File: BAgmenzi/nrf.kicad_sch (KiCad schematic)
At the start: 1 part, among them M1 *

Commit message: added libraries, other changes in sch, started pcb
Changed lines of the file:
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@@
+		)
+	)
+	(hierarchical_label "PPG_I2C{SCL, SDA}"
+		(shape bidirectional)
+		(at 63.5 114.3 180)
+		(effects
+			(font
+				(size 1.27 1.27)
+			)
+			(justify right)
 		)
 	)

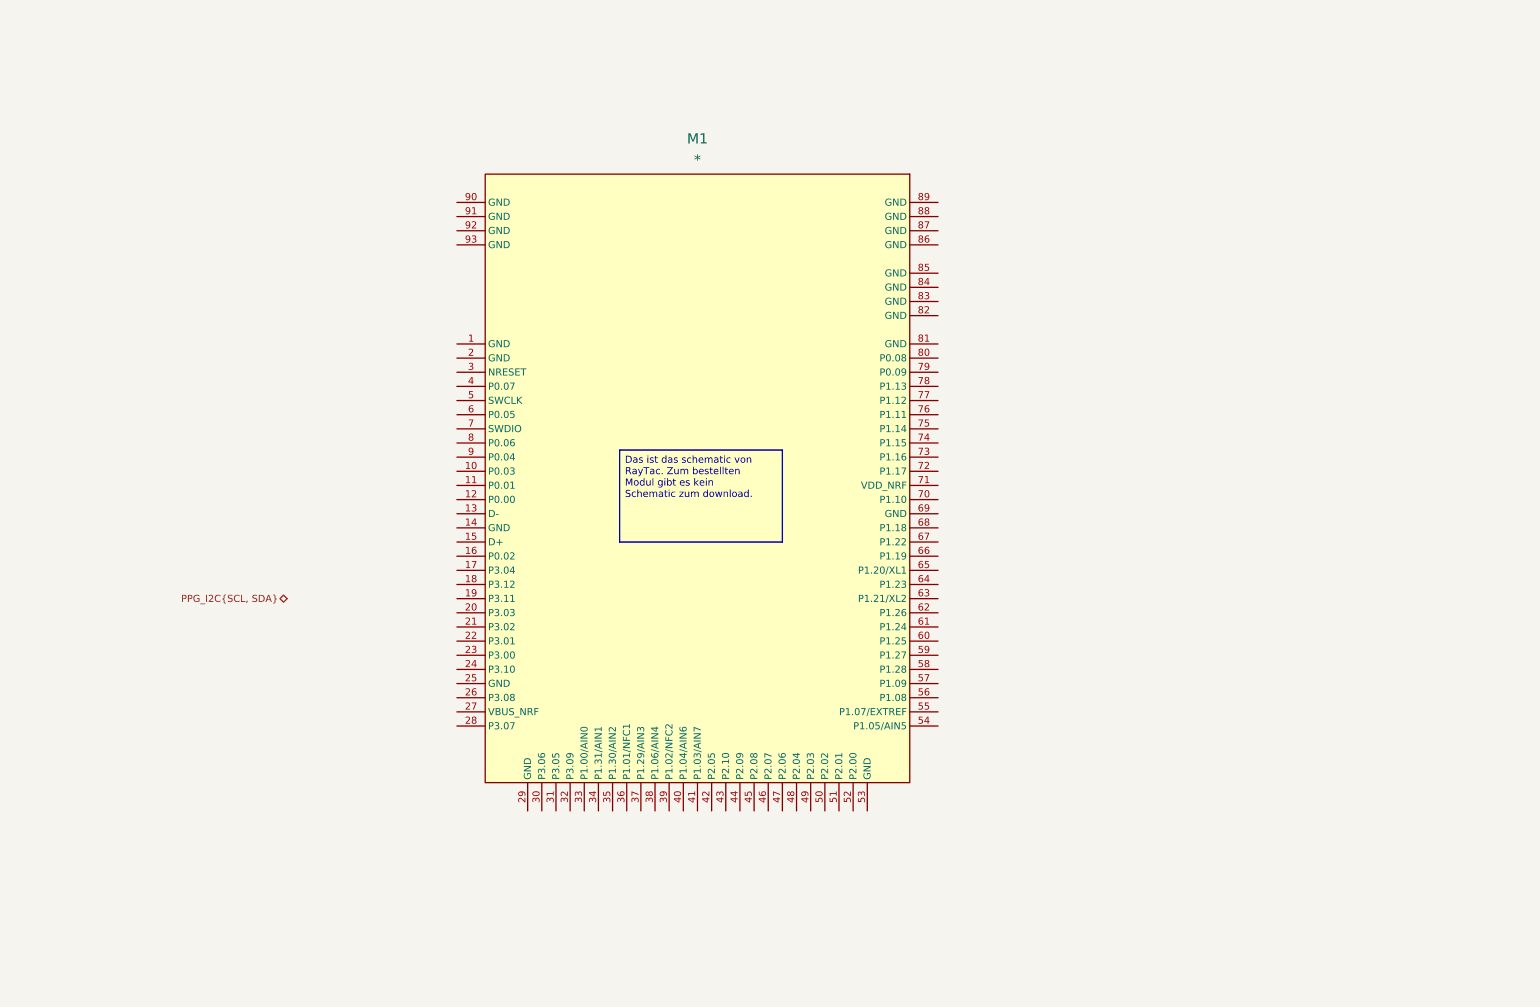
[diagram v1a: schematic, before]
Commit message: changed VRX rail and deleted U12
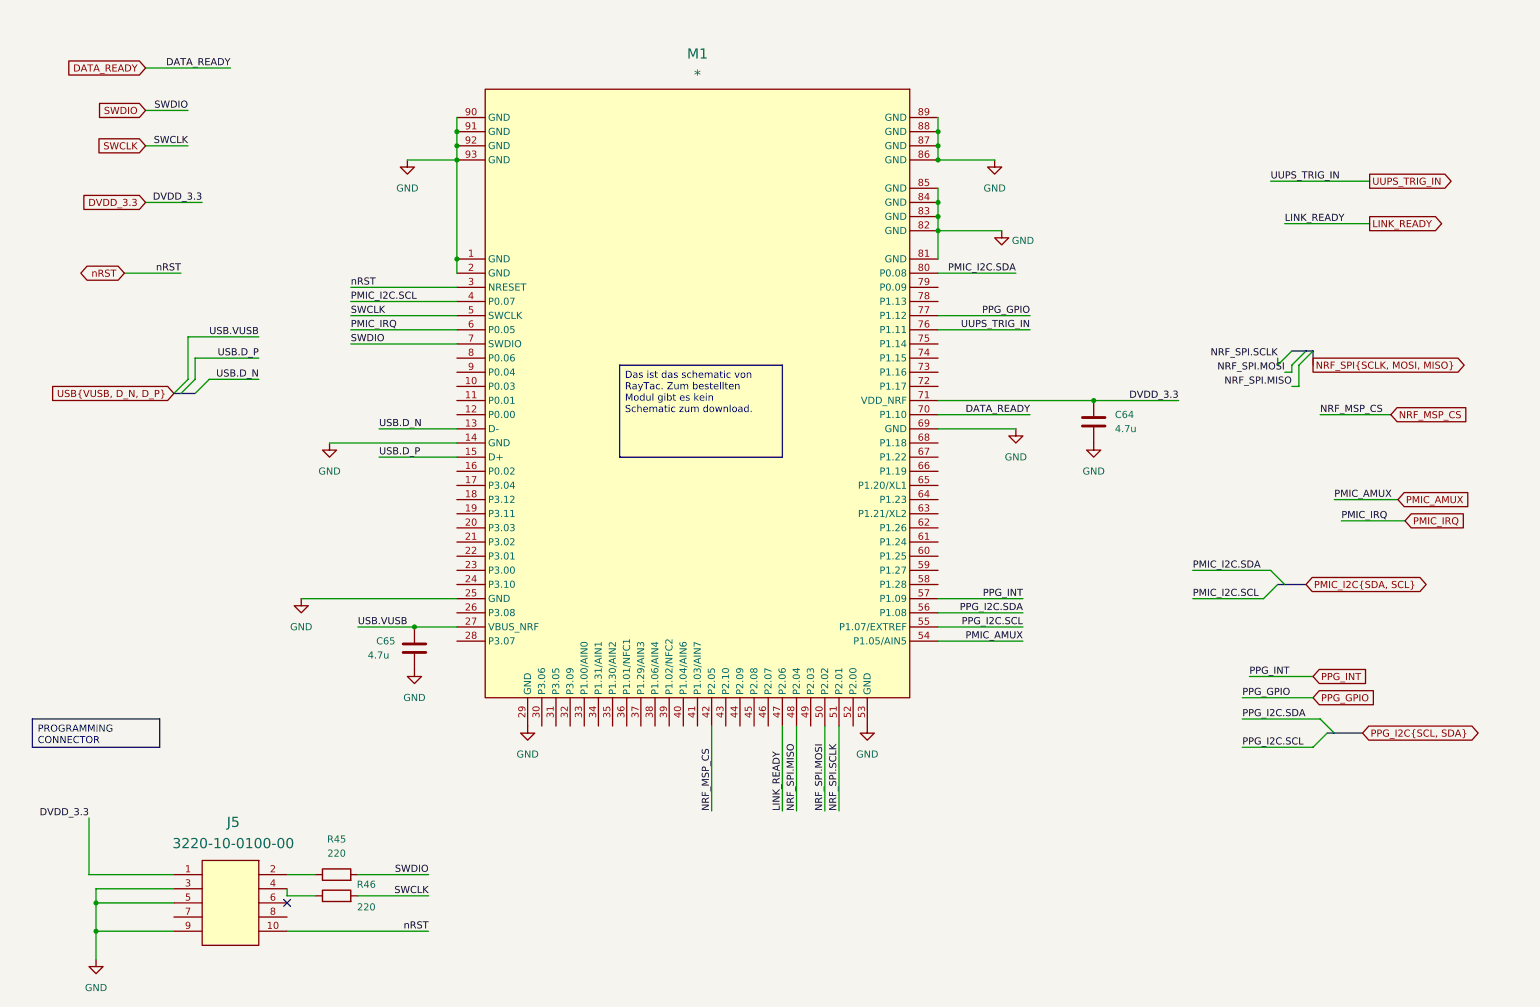
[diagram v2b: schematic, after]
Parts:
- added C64, C65: 4.7u, Capacitor_SMD:C_0402_1005Metric, symbol Device:C
- added J5: 3220-10-0100-00, EEG_PcbLib.PcbLib:CONN_3220-10-0100-00_CNC, symbol EEG_SchLib:3220-10-0100-00
- added R45, R46: 220, symbol Device:R
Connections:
- net GND: now reaches M1.1 (GND)
- net GND: now also M1.14 (GND), M1.2 (GND), M1.25 (GND), M1.29 (GND), M1.53 (GND), M1.69 (GND), M1.81 (GND), M1.82 (GND), M1.83 (GND), M1.84 (GND), M1.85 (GND), M1.86 (GND), M1.87 (GND), M1.88 (GND), M1.89 (GND), M1.90 (GND), M1.91 (GND), M1.92 (GND), M1.93 (GND), C64.2, C65.2, J5.3, J5.5, J5.9
- net USB.D_N: now reaches M1.13 (D-)
- net USB.D_P: now reaches M1.15 (D+)
- net USB.VUSB: now reaches M1.27 (VBUS_NRF)
- net USB.VUSB: now also C65.1
- net nRST: now reaches M1.3 (NRESET)
- net nRST: now also J5.10
- net PMIC_I2C.SCL: now reaches M1.4 (P0.07)
- net NRF_MSP_CS: now reaches M1.42 (P2.05)
- net LINK_READY: now reaches M1.47 (P2.06)
- net NRF_SPI.MISO: now reaches M1.48 (P2.04)
- net SWCLK: now reaches M1.5 (SWCLK)
- net SWCLK: now also R46.2
- net NRF_SPI.MOSI: now reaches M1.50 (P2.02)
- net NRF_SPI.SCLK: now reaches M1.51 (P2.01)
- net PMIC_AMUX: now reaches M1.54 (P1.05/AIN5)
- net PPG_I2C.SCL: now reaches M1.55 (P1.07/EXTREF)
- net PPG_I2C.SDA: now reaches M1.56 (P1.08)
- net PPG_INT: now reaches M1.57 (P1.09)
- net PMIC_IRQ: now reaches M1.6 (P0.05)
- net SWDIO: now reaches M1.7 (SWDIO)
- net SWDIO: now also R45.2
- net DATA_READY: now reaches M1.70 (P1.10)
- net DVDD_3.3: now reaches M1.71 (VDD_NRF)
- net DVDD_3.3: now also C64.1, J5.1
- net UUPS_TRIG_IN: now reaches M1.76 (P1.11)
- net PPG_GPIO: now reaches M1.77 (P1.12)
- net PMIC_I2C.SDA: now reaches M1.80 (P0.08)
- new net: J5.4, R46.1
- new net: J5.2, R45.1
- no-connect marks 0 -> 1
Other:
- moved on the sheet: M1

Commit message: started layout, front v backside
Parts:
- J5: footprint EEG_PcbLib.PcbLib:CONN_3220-10-0100-00_CNC -> EEG_PcbLib:CONN_3220-10-0100-00_CNC
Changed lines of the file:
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@@
 			)
 		)
-		(property "Footprint" "EEG_PcbLib.PcbLib:CONN_3220-10-0100-00_CNC"
+		(property "Footprint" "EEG_PcbLib:CONN_3220-10-0100-00_CNC"
 			(at 53.34 168.91 0)
 			(effects

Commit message: started routing, changed enable signals to nRF
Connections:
- net HV_NEG_EN: now reaches M1.72 (P1.17)
- net HV_POS_EN: now reaches M1.73 (P1.16)
- net HV_PWR_EN: now reaches M1.74 (P1.15)
- net VRX_EN: now reaches M1.75 (P1.14)

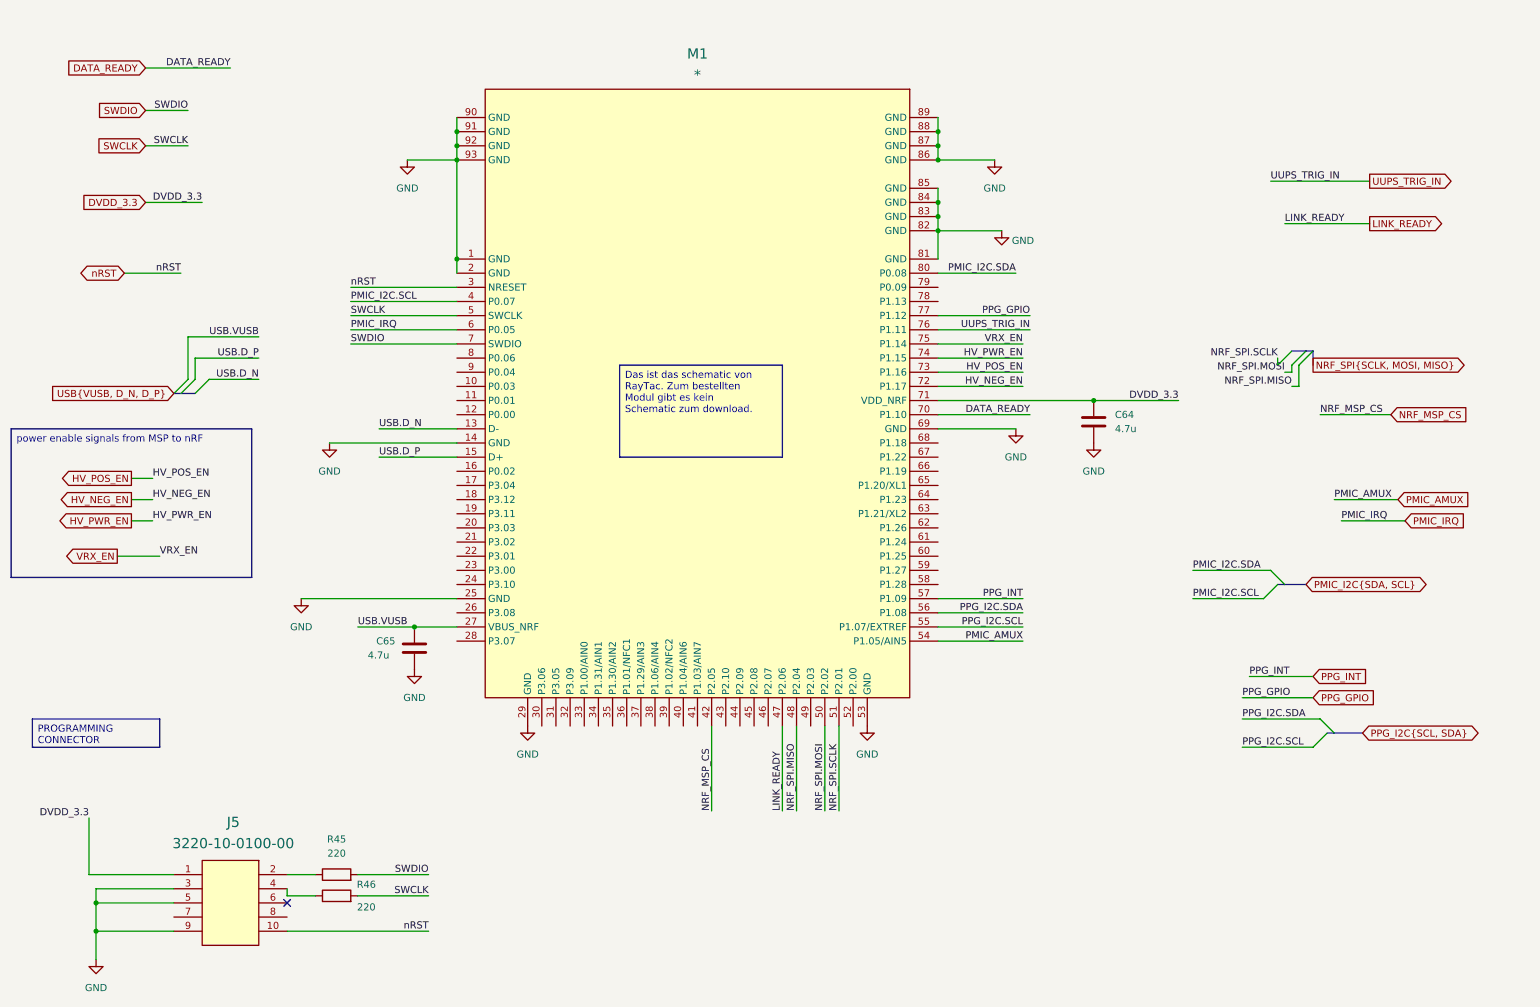
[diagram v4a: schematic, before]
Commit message: routed msp and nrf
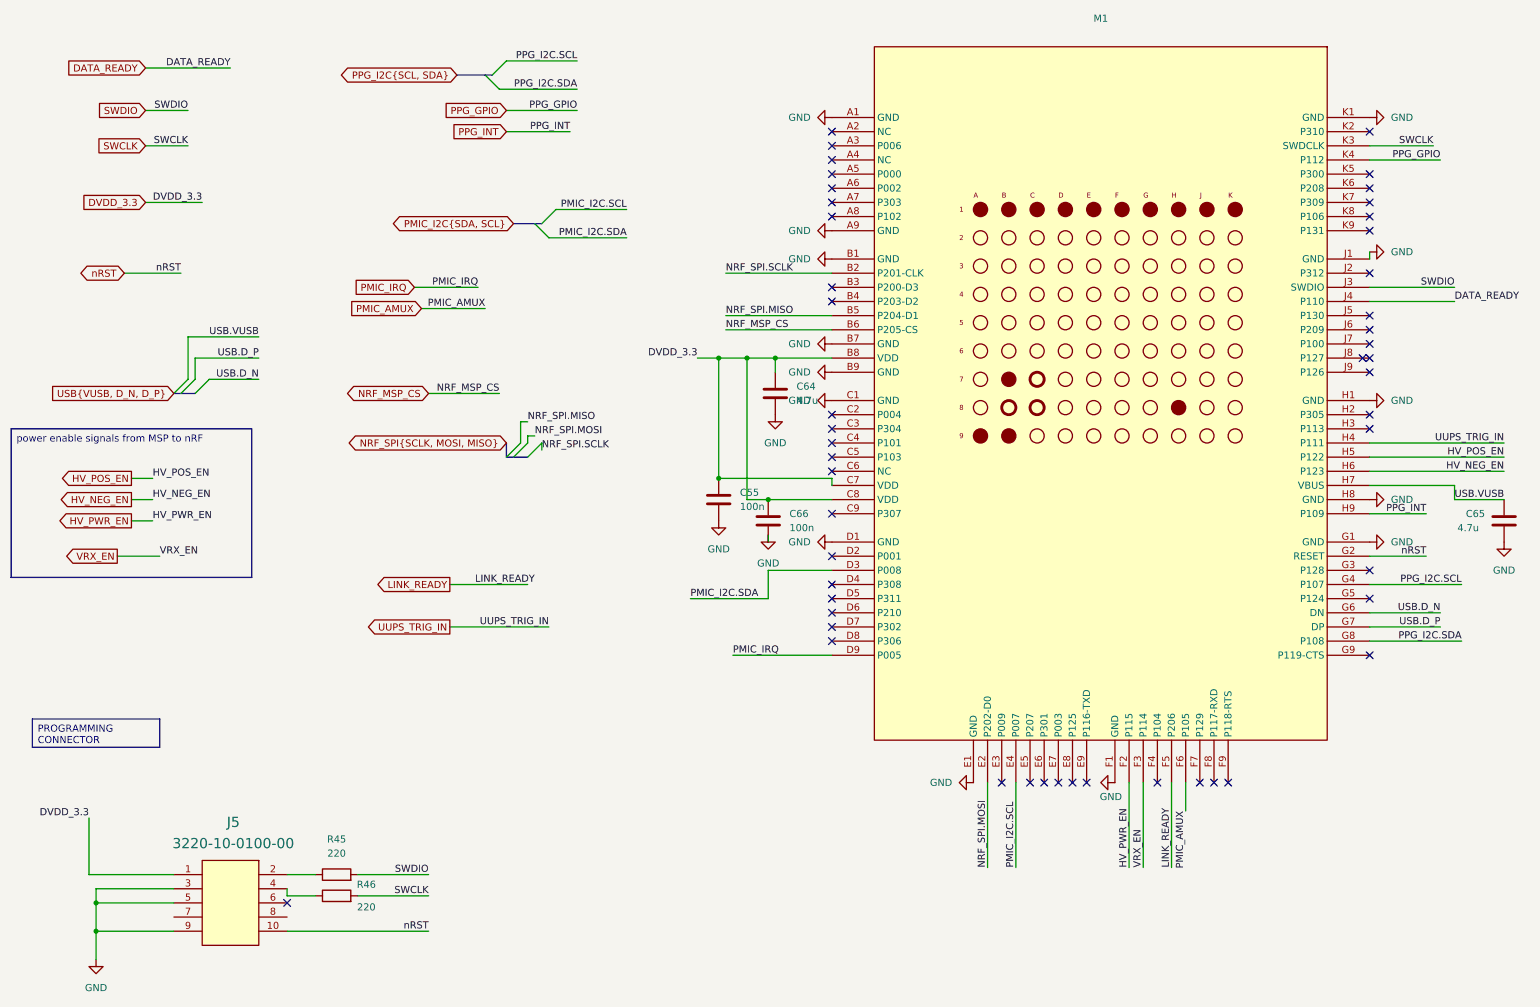
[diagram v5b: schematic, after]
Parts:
- removed M1: *, AN54LM-20_P20, symbol AN54LM-20_SCH-260723:AN54LM-20_P20
- added C55, C66: 100n, Capacitor_SMD:C_0402_1005Metric, symbol Device:C
- added M1: ~, nRFPCB:BM20-C, symbol nRF_LIB-altium-import:root_0_NRF51822-44P_130_*
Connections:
- net DATA_READY: now also M1.J4 (P110)
- net DVDD_3.3: now also C55.1, C66.1, M1.B8 (VDD), M1.C7 (VDD), M1.C8 (VDD)
- net GND: now also C55.2, C66.2, M1.A1 (GND), M1.A9 (GND), M1.B1 (GND), M1.B7 (GND), M1.B9 (GND), M1.C1 (GND), M1.D1 (GND), M1.E1 (GND), M1.F1 (GND), M1.G1 (GND), M1.H1 (GND), M1.H8 (GND), M1.J1 (GND), M1.K1 (GND)
- net HV_NEG_EN: now also M1.H6 (P123)
- net HV_POS_EN: now also M1.H5 (P122)
- net HV_PWR_EN: now also M1.F2 (P115)
- net LINK_READY: now also M1.F5 (P206)
- net NRF_MSP_CS: now also M1.B6 (P205-CS)
- net NRF_SPI.MISO: now also M1.B5 (P204-D1)
- net NRF_SPI.MOSI: now also M1.E2 (P202-D0)
- net NRF_SPI.SCLK: now also M1.B2 (P201-CLK)
- net PMIC_AMUX: now also M1.F6 (P105)
- net PMIC_I2C.SCL: now also M1.E4 (P007)
- net PMIC_I2C.SDA: now also M1.D3 (P008)
- net PMIC_IRQ: now also M1.D9 (P005)
- net PPG_GPIO: now also M1.K4 (P112)
- net PPG_I2C.SCL: now also M1.G4 (P107)
- net PPG_I2C.SDA: now also M1.G8 (P108)
- net PPG_INT: now also M1.H9 (P109)
- net SWCLK: now also M1.K3 (SWDCLK)
- net SWDIO: now also M1.J3 (SWDIO)
- net USB.D_N: now also M1.G6 (DN)
- net USB.D_P: now also M1.G7 (DP)
- net USB.VUSB: now also M1.H7 (VBUS)
- net UUPS_TRIG_IN: now also M1.H4 (P111)
- net VRX_EN: now also M1.F3 (P114)
- net nRST: now also M1.G2 (RESET)
- no-connect marks 1 -> 50
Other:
- moved on the sheet: C64, C65

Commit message: powerplanes
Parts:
- J5: footprint EEG_PcbLib:CONN_3220-10-0100-00_CNC -> Connector_PinHeader_1.27mm:PinHeader_2x05_P1.27mm_Vertical_SMD
- R45, R46: footprint (none) -> EEG_PcbLib:0402
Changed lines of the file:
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@@
 			)
 		)
-		(property "Footprint" ""
+		(property "Footprint" "EEG_PcbLib:0402"
 			(at 72.39 169.418 90)
 			(effects
@@
 			)
 		)
-		(property "Footprint" ""
+		(property "Footprint" "EEG_PcbLib:0402"
 			(at 72.39 165.608 90)
 			(effects
@@
 			)
 		)
-		(property "Footprint" "EEG_PcbLib:CONN_3220-10-0100-00_CNC"
+		(property "Footprint" "Connector_PinHeader_1.27mm:PinHeader_2x05_P1.27mm_Vertical_SMD"
 			(at 53.34 168.91 0)
 			(effects

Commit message: DRC correfted all red falgs
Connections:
- no-connect marks 50 -> 52
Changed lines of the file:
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@@
+	)
+	(no_connect
+		(at 43.18 171.45)
 	)
 	(no_connect
@@
 	)
 	(no_connect
+		(at 63.5 171.45)
+	)
+	(no_connect
